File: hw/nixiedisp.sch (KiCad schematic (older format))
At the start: 58 parts, among them J1 12VDC IN, J2 USB_B_Micro, J3 AVR-ISP-6, J4 pwr sw, J5 HRLEDS, Q1 MMBTA55, Q2 IRF540N, U1 ATmega328P-AU, U10 IN14, U11 IN14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

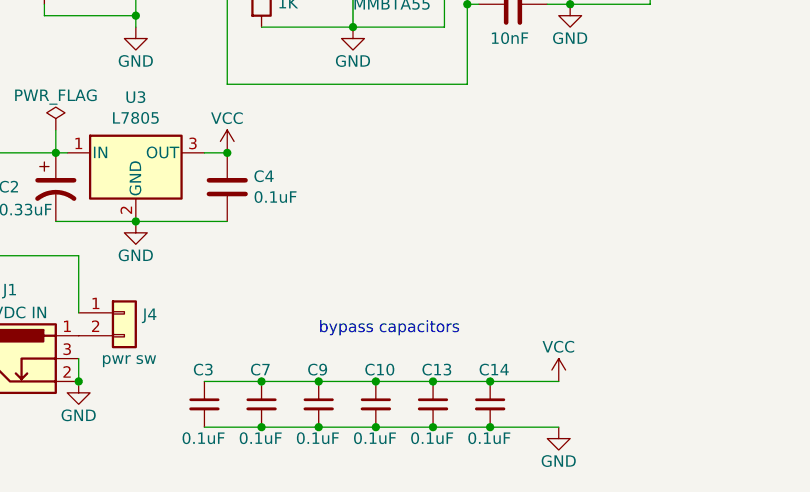
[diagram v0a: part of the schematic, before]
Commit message: started on the firmware, added BOM
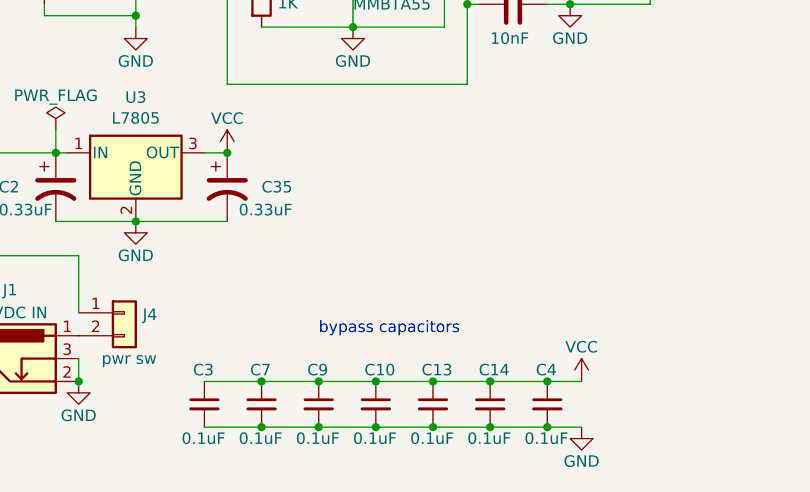
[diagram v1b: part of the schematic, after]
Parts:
- removed C4: 0.1uF, Capacitor_SMD:C_0805_2012Metric_Pad1.15x1.40mm_HandSolder, symbol Device:C
- added C35: 0.33uF, Capacitor_SMD:CP_Elec_4x5.4, symbol Device:CP1
- added C4: 0.1uF, Capacitor_SMD:C_0805_2012Metric_Pad1.15x1.40mm_HandSolder, symbol Device:C_Small
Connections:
- net GND: now also C35.2, C4.2
- net VCC: now also C35.1, C4.1
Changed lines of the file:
@@
 $EndComp
 Connection ~ 800  8200
-$Comp
-L Device:C C4
-U 1 1 61166BC4
-P 1850 9900
-F 0 "C4" H 1965 9946 50  0000 L CNN
-F 1 "0.1uF" H 1965 9855 50  0000 L CNN
-F 2 "Capacitor_SMD:C_0805_2012Metric_Pad1.15x1.40mm_HandSolder" H 1888 9750 50  0001 C CNN
-F 3 "~" H 1850 9900 50  0001 C CNN
-	1    1850 9900
-	1    0    0    -1
-$EndComp
-Connection ~ 1850 9750
 Wire Wire Line
 	3350 8800 2900 8800
@@
 L power:GND #PWR019
 U 1 1 61B0EE96
-P 3300 10950
-F 0 "#PWR019" H 3300 10700 50  0001 C CNN
-F 1 "GND" H 3300 10800 50  0000 C CNN
-F 2 "" H 3300 10950 50  0001 C CNN
-F 3 "" H 3300 10950 50  0001 C CNN
-	1    3300 10950
+P 3400 10950
+F 0 "#PWR019" H 3400 10700 50  0001 C CNN
+F 1 "GND" H 3400 10800 50  0000 C CNN
+F 2 "" H 3400 10950 50  0001 C CNN
+F 3 "" H 3400 10950 50  0001 C CNN
+	1    3400 10950
 	1    0    0    -1
 $EndComp
@@
 L power:VCC #PWR018
 U 1 1 61B3194F
-P 3300 10750
-F 0 "#PWR018" H 3300 10600 50  0001 C CNN
-F 1 "VCC" H 3300 10900 50  0000 C CNN
-F 2 "" H 3300 10750 50  0001 C CNN
-F 3 "" H 3300 10750 50  0001 C CNN
-	1    3300 10750
+P 3400 10750
+F 0 "#PWR018" H 3400 10600 50  0001 C CNN
+F 1 "VCC" H 3400 10900 50  0000 C CNN
+F 2 "" H 3400 10750 50  0001 C CNN
+F 3 "" H 3400 10750 50  0001 C CNN
+	1    3400 10750
 	1    0    0    -1
 $EndComp
@@
 	3700 8400 3700 8500
 Wire Wire Line
-	3000 10750 3300 10750
+	3000 10750 3250 10750
 Connection ~ 3000 10750
 Wire Wire Line
-	3000 10950 3300 10950
+	3000 10950 3250 10950
 Connection ~ 3000 10950
 Text Notes 2250 10550 0    50   ~ 0
@@
 Wire Wire Line
 	3400 750  3400 850
+$Comp
+L Device:C_Small C4
+U 1 1 5FF08D11
+P 3250 10850
+F 0 "C4" H 3200 11000 50  0000 L CNN
+F 1 "0.1uF" H 3150 10700 50  0000 L CNN
+F 2 "Capacitor_SMD:C_0805_2012Metric_Pad1.15x1.40mm_HandSolder" H 3250 10850 50  0001 C CNN
+F 3 "~" H 3250 10850 50  0001 C CNN
+	1    3250 10850
+	1    0    0    -1
+$EndComp
+Connection ~ 3250 10750
+Wire Wire Line
+	3250 10750 3400 10750
+Connection ~ 3250 10950
+Wire Wire Line
+	3250 10950 3400 10950
+$Comp
+L Device:CP1 C35
+U 1 1 5FF65C5D
+P 1850 9900
+F 0 "C35" H 2000 9900 50  0000 L CNN
+F 1 "0.33uF" H 1900 9800 50  0000 L CNN
+F 2 "Capacitor_SMD:CP_Elec_4x5.4" H 1850 9900 50  0001 C CNN
+F 3 "~" H 1850 9900 50  0001 C CNN
+	1    1850 9900
+	1    0    0    -1
+$EndComp
+Connection ~ 1850 9750
 $EndSCHEMATC

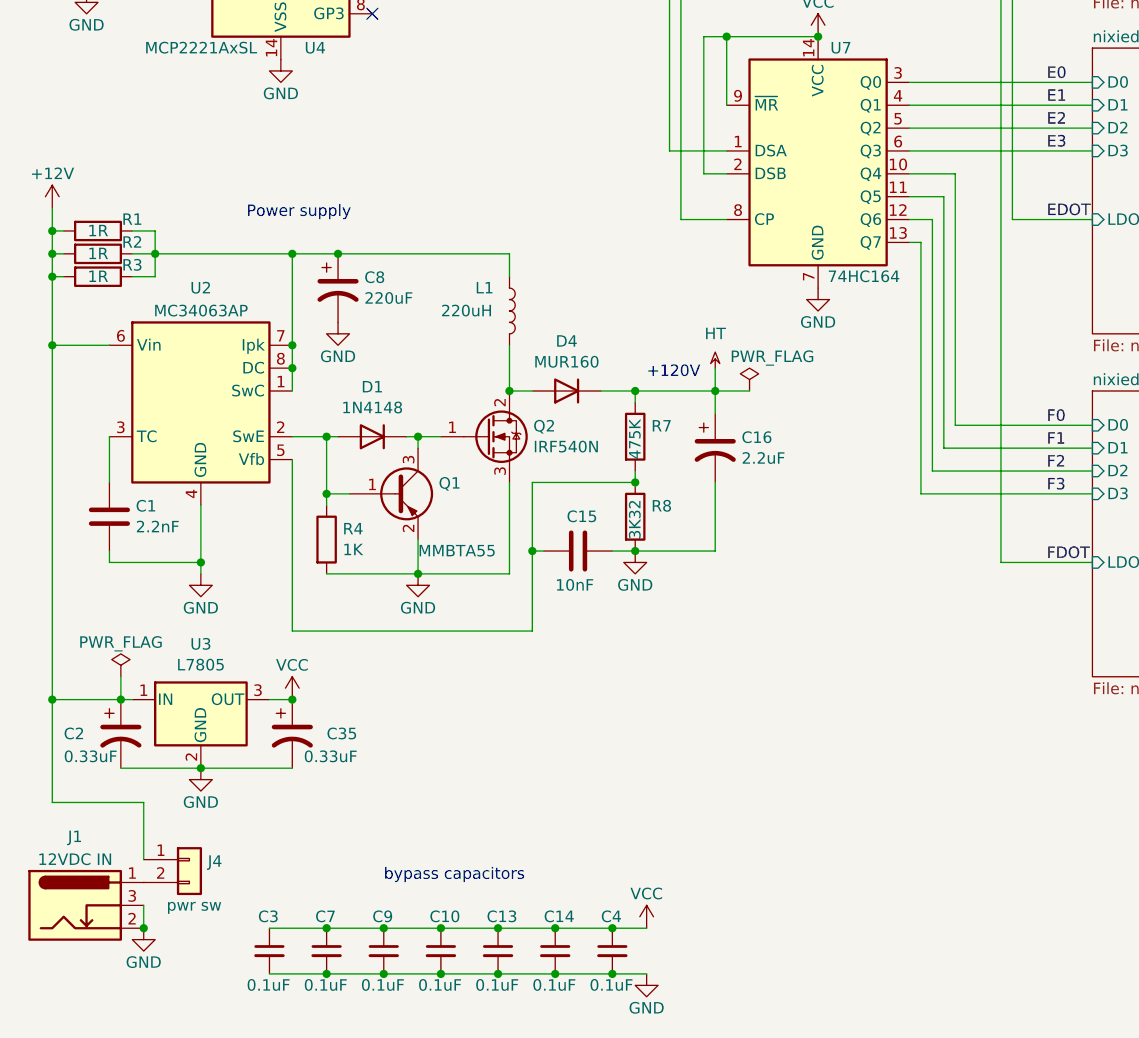
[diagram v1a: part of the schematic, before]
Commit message: - fixed mistakes in the schematic - updated the PCB for the fixes - in process of adding a proper serial port with a max232
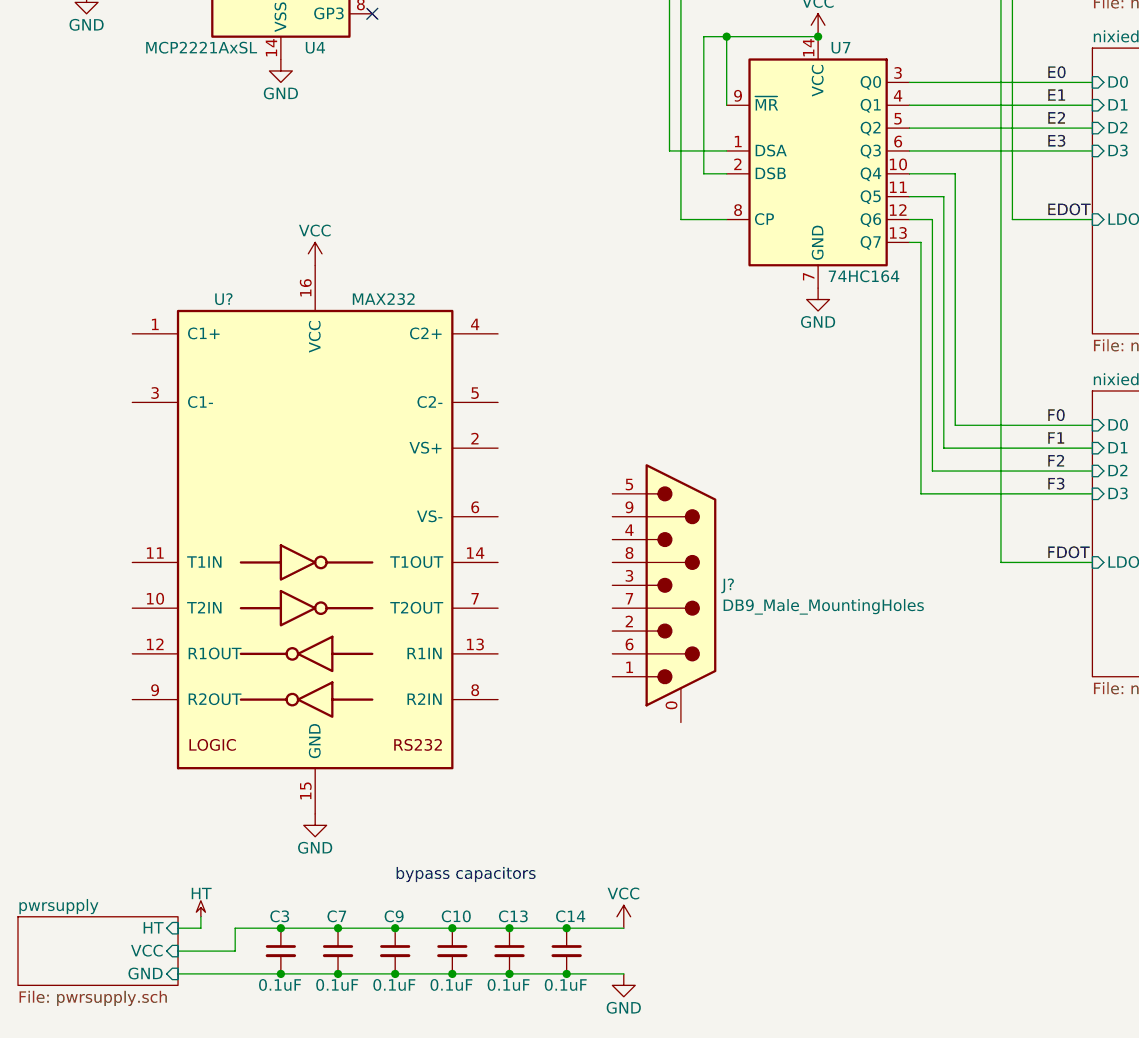
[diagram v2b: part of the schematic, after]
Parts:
- removed C1: 2.2nF, Capacitor_SMD:C_0805_2012Metric_Pad1.15x1.40mm_HandSolder, symbol Device:C
- removed C15: 10nF, Capacitor_SMD:C_0805_2012Metric_Pad1.15x1.40mm_HandSolder, symbol Device:C
- removed C16: 2.2uF, Capacitor_THT:CP_Radial_D6.3mm_P2.50mm, symbol Device:CP1
- removed C2, C35: 0.33uF, Capacitor_SMD:CP_Elec_4x5.4, symbol Device:CP1
- removed C4: 0.1uF, Capacitor_SMD:C_0805_2012Metric_Pad1.15x1.40mm_HandSolder, symbol Device:C_Small
- removed C8: 220uF, Capacitor_SMD:CP_Elec_8x10, symbol Device:CP1
- removed D1: 1N4148, Diode_SMD:D_0805_2012Metric_Pad1.15x1.40mm_HandSolder, symbol Diode:1N4148
- removed D4: MUR160, Diode_THT:D_DO-15_P12.70mm_Horizontal, symbol Device:D
- removed J1: 12VDC IN, Connector_BarrelJack:BarrelJack_Horizontal, symbol Connector:Barrel_Jack_Switch
- removed J4: pwr sw, Connector_PinHeader_2.54mm:PinHeader_1x02_P2.54mm_Vertical, symbol Connector_Generic:Conn_01x02
- removed L1: 220uH, Inductor_THT:L_Radial_D8.7mm_P5.00mm_Fastron_07HCP, symbol Device:L
- removed Q1: MMBTA55, Package_TO_SOT_SMD:SOT-23, symbol nixiedisp:MMBTA55
- removed Q2: IRF540N, Package_TO_SOT_THT:TO-220-3_Vertical, symbol Transistor_FET:IRF540N
- removed R1, R2, R3: 1R, Resistor_SMD:R_0805_2012Metric_Pad1.15x1.40mm_HandSolder, symbol Device:R
- removed R4: 1K, Resistor_SMD:R_0805_2012Metric_Pad1.15x1.40mm_HandSolder, symbol Device:R
- removed R7: 475K, Resistor_SMD:R_0805_2012Metric_Pad1.15x1.40mm_HandSolder, symbol Device:R
- removed R8: 3K32, Resistor_SMD:R_0805_2012Metric_Pad1.15x1.40mm_HandSolder, symbol Device:R
- removed U2: MC34063AP, Package_DIP:DIP-8_W7.62mm, symbol Regulator_Switching:MC34063AP
- removed U3: L7805, Package_TO_SOT_THT:TO-220-3_Vertical, symbol Regulator_Linear:L7805
- added J?: DB9_Male_MountingHoles, symbol Connector:DB9_Male_MountingHoles
- added U?: MAX232, symbol Interface_UART:MAX232
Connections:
- net GND: now also U?.15 (GND)
- net VCC: now also U?.16 (VCC)
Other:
- note removed: "+120V"
- note removed: "Power supply"
- moved on the sheet: C10, C13, C14, C3, C7, C9

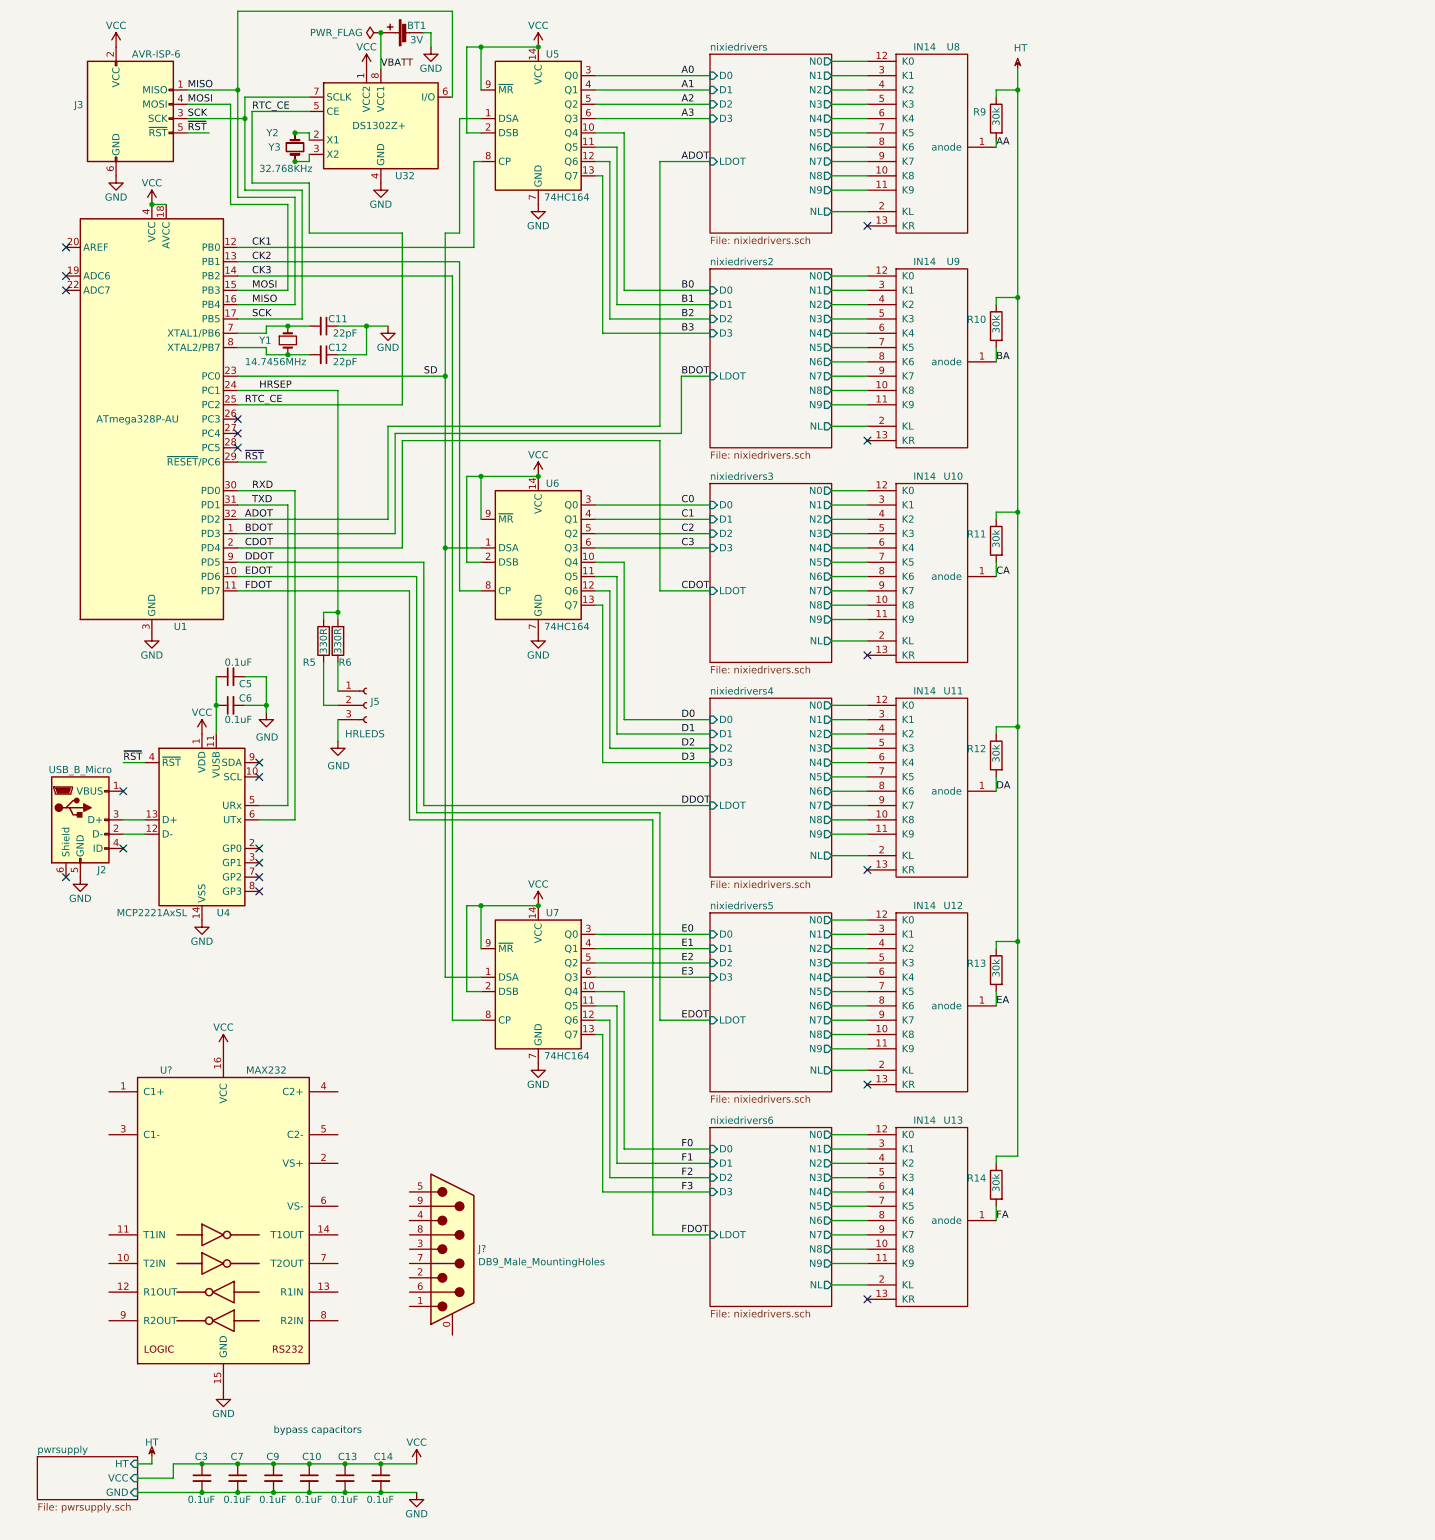
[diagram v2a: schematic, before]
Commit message: lots of changes, redesigning most of the PCB
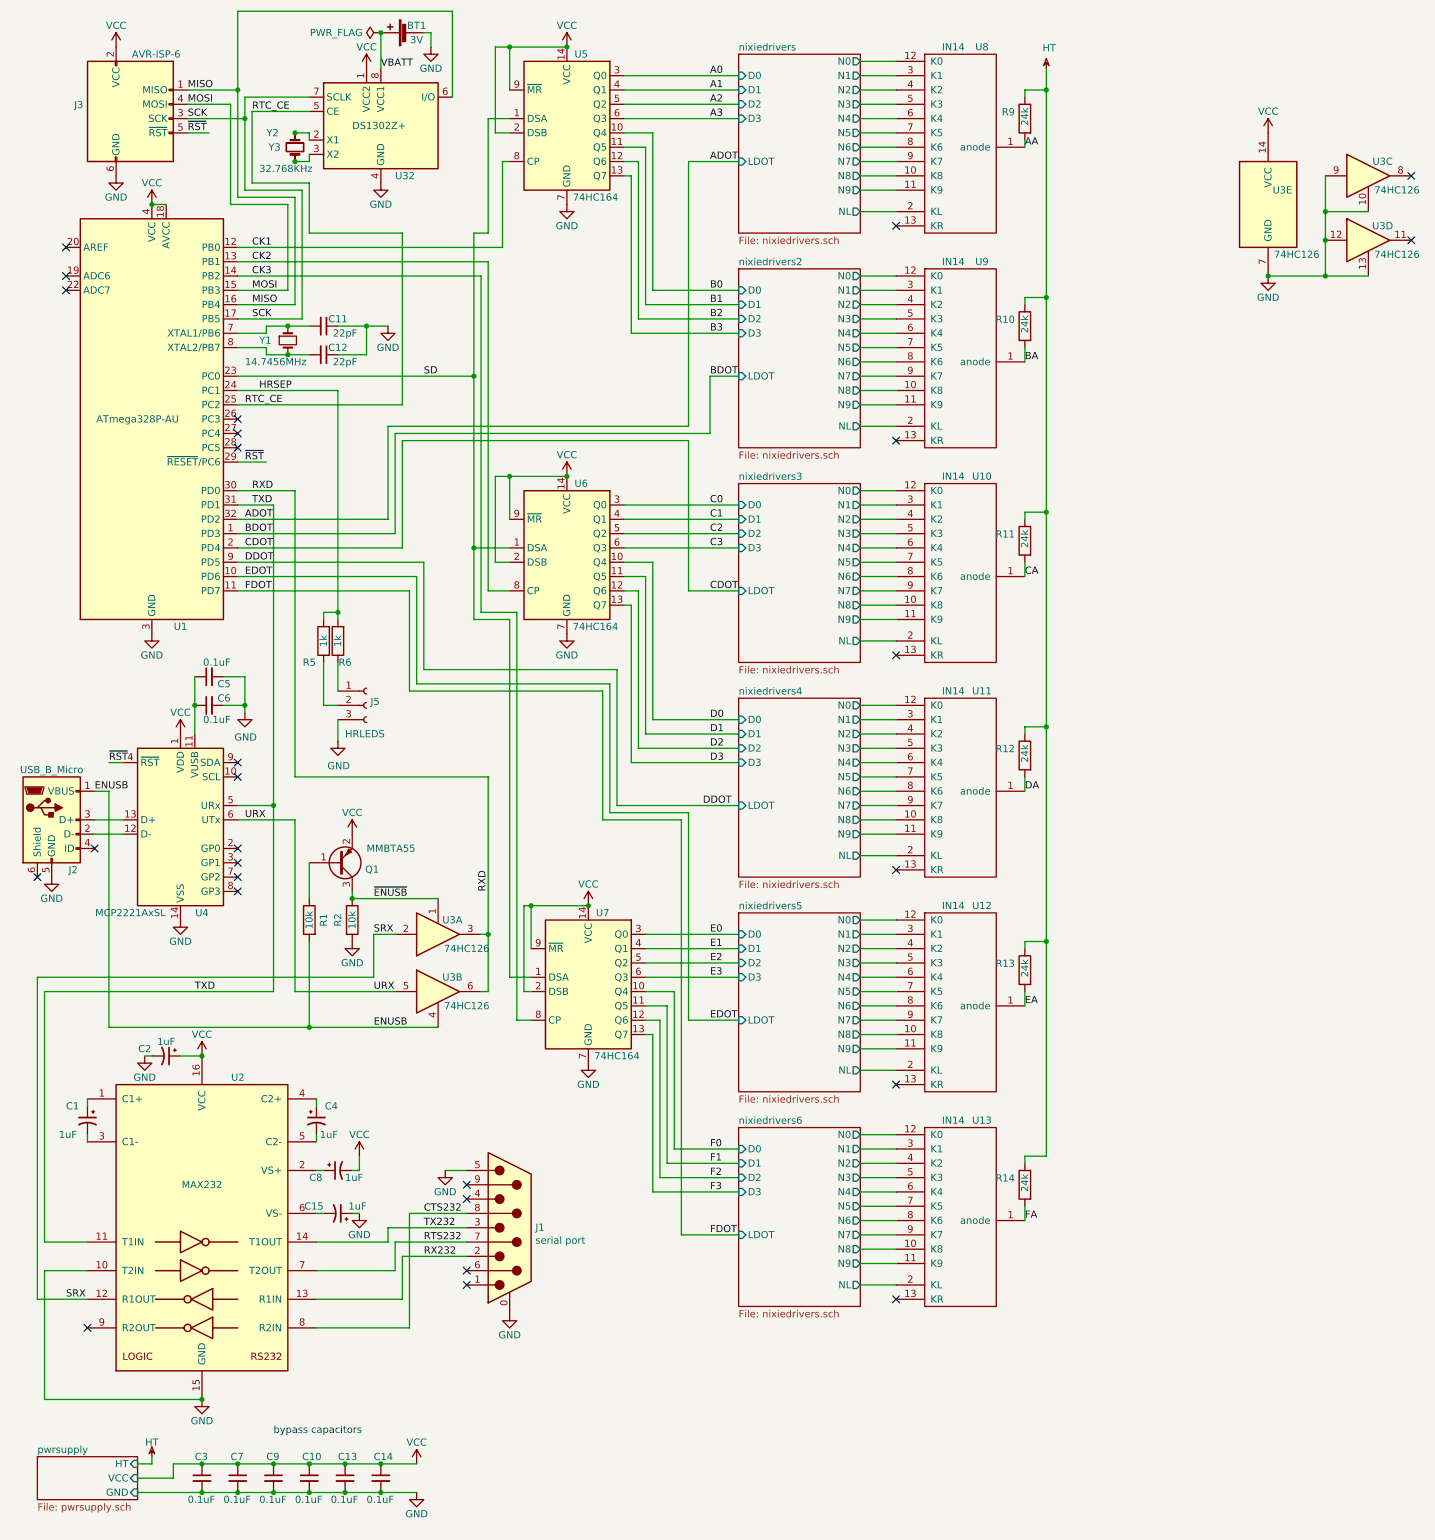
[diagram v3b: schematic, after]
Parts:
- removed U?: MAX232, symbol Interface_UART:MAX232
- added C1, C15, C2, C4, C8: 1uF, Capacitor_SMD:CP_Elec_4x3.9, symbol Device:CP1_Small
- added Q1: MMBTA55, Package_TO_SOT_SMD:SOT-23, symbol nixiedisp:MMBTA55
- added R1, R2: 10k, Resistor_SMD:R_0805_2012Metric_Pad1.15x1.40mm_HandSolder, symbol Device:R
- added U2: MAX232, Package_SO:SOIC-16_3.9x9.9mm_P1.27mm, symbol Interface_UART:MAX232
- added U3: 74HC126, Package_SO:SOIC-14_3.9x8.7mm_P1.27mm, symbol 74xx:74LS126
- J1: renamed from J?; value DB9_Male_MountingHoles -> serial port; footprint (none) -> Connector_Dsub:DSUB-9_Male_Horizontal_P2.77x2.84mm_EdgePinOffset7.70mm_Housed_MountingHolesOffset9.12mm
- R10, R11, R12, R13, R14, R9: value 30k -> 24k
- R5, R6: value 330R -> 1k
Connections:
- net GND: now also J1.0 (PAD), J1.5, C15.1, C2.2, R2.2, U2.10 (T2IN), U2.15 (GND), U3.10, U3.12, U3.13, U3.7 (GND), U3.9
- net RXD: now also U3.3, U3.6; no longer U4.6 (UTx)
- net TXD: now also U2.11 (T1IN)
- net VCC: now also C2.1, C8.2, Q1.2 (E), U2.16 (VCC), U3.14 (VCC)
- net RX232: now reaches J1.2
- net RX232: now also U2.13 (R1IN)
- net TX232: now reaches J1.3
- net TX232: now also U2.14 (T1OUT)
- net RTS232: now reaches J1.7
- net RTS232: now also U2.7 (T2OUT)
- net CTS232: now reaches J1.8
- net CTS232: now also U2.8 (R2IN)
- net ENUSB: now reaches J2.1 (VBUS)
- net ENUSB: now also R1.2, U3.4
- new net: C1.1, U2.1 (C1+)
- new net: C1.2, U2.3 (C1-)
- new net: C4.1, U2.4 (C2+)
- new net: C4.2, U2.5 (C2-)
- new net: C8.1, U2.2 (VS+)
- new net: C15.2, U2.6 (VS-)
- new net: Q1.1 (B), R1.1
- new net SRX: U2.12 (R1OUT), U3.2
- new net URX: U3.5, U4.6 (UTx)
- new net ~ENUSB: Q1.3 (C), R2.1, U3.1
- no-connect marks 21 -> 27
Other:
- moved on the sheet: C5, C6, J1, J2, R10, R11, R12, R13, R14, R9, U10, U11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
